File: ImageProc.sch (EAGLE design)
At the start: 114 parts, among them IC1 XC61GC3002HR-G, IC10 AT45DB642D-CNU, IC2 MIC5335-SPYMT, IC3 MIC5335-JGYMT, IC5 AT86RF233-ZU, IC6 LTC6088, IC7 DRV8833RTY, IC8 DRV8833RTY, IC9 MPU-6000, P1 BAT+, P10 MD2, P11 EXT1, P12 EXT2, P13 EXT3, P14 EXT4, P16 EXT5, P2 BAT-, P3 MA1, P4 MA2, P5 MB1, P6 MB2, P7 MC1, P8 MC2, P9 MD1, U1 CY8C5688LTI-LP086

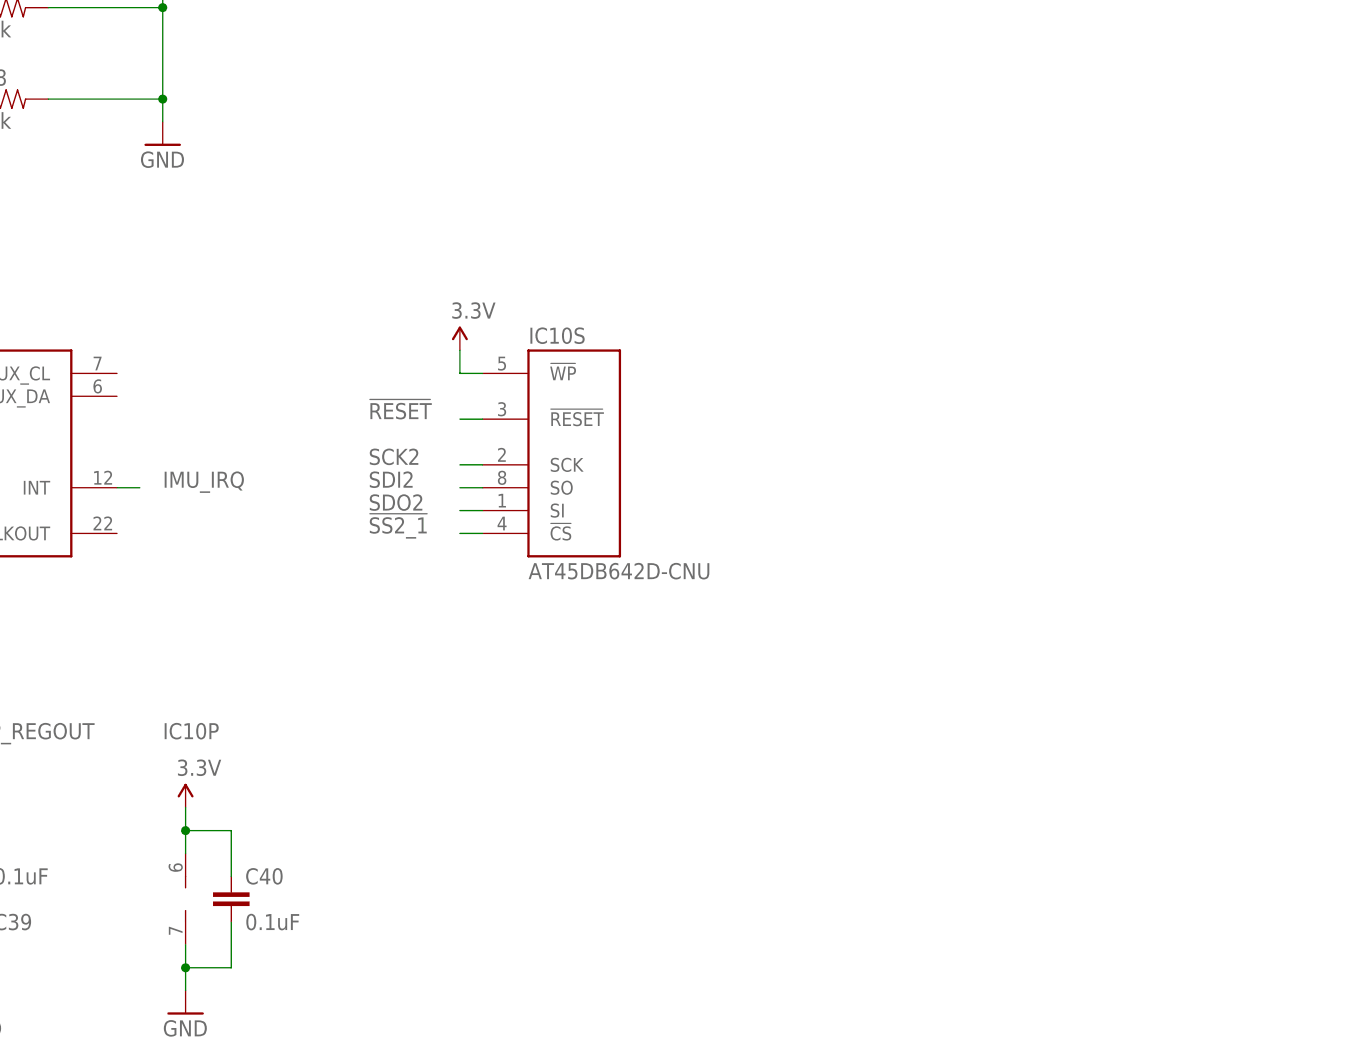
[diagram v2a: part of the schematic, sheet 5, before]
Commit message: Removed flash, ripping up more routing, added SD card
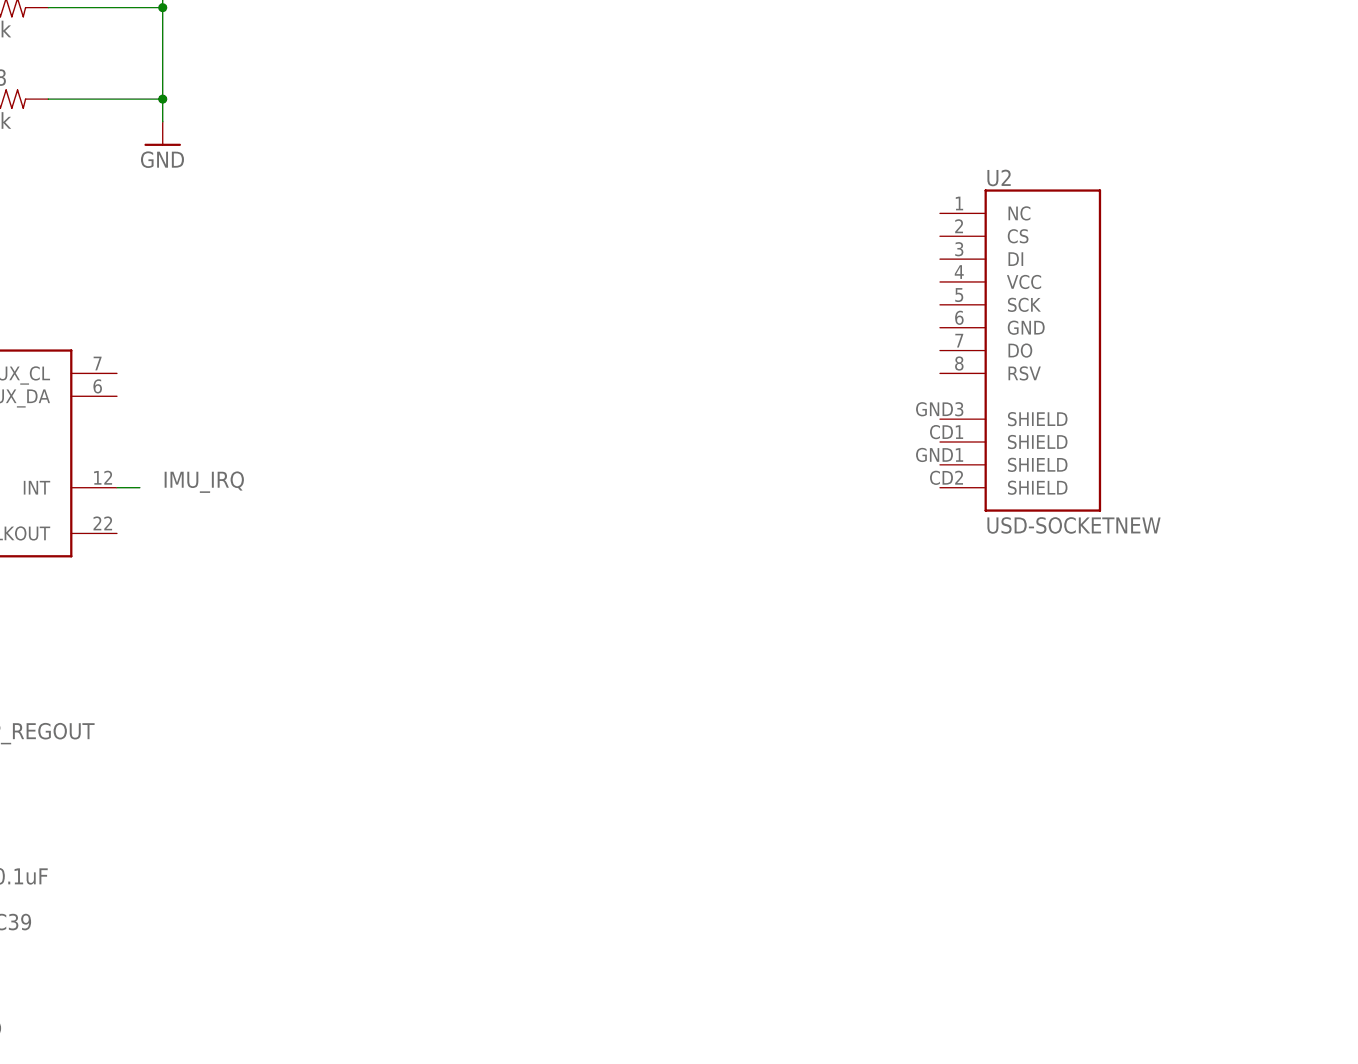
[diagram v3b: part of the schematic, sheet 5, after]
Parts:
- removed C40: 0.1uF, biomimetic:CAP0402-CAP
- removed IC10: AT45DB642D-CNU, biomimetic:AT45DB642D-CNU
- added U2: USD-SOCKETNEW, SparkFun-Connectors:USD-SOCKETNEW
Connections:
- removed net !SS2_1: IC10S.!CS
- net !RESET: no longer IC10S.!RESET
- net 3.3V: no longer C40.1, IC10P.V+, IC10S.!WP
- net GND: no longer C40.2, IC10P.V-
- net SCK2: no longer IC10S.SCK
- net SDI2: no longer IC10S.SO
- net SDO2: no longer IC10S.SI
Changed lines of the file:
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@@
 <layer number="108" name="tplace-old" color="10" fill="1" visible="no" active="yes"/>
 <layer number="109" name="ref-old" color="11" fill="1" visible="no" active="yes"/>
+<layer number="110" name="fp0" color="7" fill="1" visible="yes" active="yes"/>
+<layer number="111" name="LPC17xx" color="7" fill="1" visible="yes" active="yes"/>
+<layer number="112" name="tSilk" color="7" fill="1" visible="yes" active="yes"/>
+<layer number="113" name="IDFDebug" color="4" fill="1" visible="yes" active="yes"/>
 <layer number="116" name="Patch_BOT" color="9" fill="4" visible="no" active="yes"/>
 <layer number="121" name="_tsilk" color="7" fill="1" visible="no" active="yes"/>
 <layer number="122" name="_bsilk" color="7" fill="1" visible="no" active="yes"/>
+<layer number="123" name="tTestmark" color="7" fill="1" visible="yes" active="yes"/>
+<layer number="124" name="bTestmark" color="7" fill="1" visible="yes" active="yes"/>
 <layer number="125" name="_tNames" color="7" fill="1" visible="no" active="yes"/>
+<layer number="126" name="_bNames" color="7" fill="1" visible="yes" active="yes"/>
+<layer number="127" name="_tValues" color="7" fill="1" visible="yes" active="yes"/>
+<layer number="128" name="_bValues" color="7" fill="1" visible="yes" active="yes"/>
+<layer number="131" name="tAdjust" color="7" fill="1" visible="yes" active="yes"/>
+<layer number="132" name="bAdjust" color="7" fill="1" visible="yes" active="yes"/>
 <layer number="144" name="Drill_legend" color="7" fill="1" visible="no" active="yes"/>
+<layer number="150" name="Notes" color="7" fill="1" visible="yes" active="yes"/>
 <layer number="151" name="HeatSink" color="7" fill="1" visible="no" active="yes"/>
+<layer number="152" name="_bDocu" color="7" fill="1" visible="yes" active="yes"/>
+<layer number="153" name="FabDoc1" color="7" fill="1" visible="yes" active="yes"/>
+<layer number="154" name="FabDoc2" color="7" fill="1" visible="yes" active="yes"/>
+<layer number="155" name="FabDoc3" color="7" fill="1" visible="yes" active="yes"/>
 <layer number="199" name="Contour" color="7" fill="1" visible="yes" active="yes"/>
 <layer number="200" name="200bmp" color="1" fill="10" visible="no" active="yes"/>
@@
 <layer number="223" name="223bmp" color="24" fill="1" visible="no" active="no"/>
 <layer number="224" name="224bmp" color="25" fill="1" visible="no" active="no"/>
+<layer number="248" name="Housing" color="7" fill="1" visible="yes" active="yes"/>
+<layer number="249" name="Edge" color="7" fill="1" visible="yes" active="yes"/>
 <layer number="250" name="Descript" color="3" fill="1" visible="no" active="no"/>
 <layer number="251" name="SMDround" color="12" fill="11" visible="no" active="no"/>
@@
 <part name="P+8" library="biomimetic" deviceset="3.3V" device=""/>
 <part name="IC6" library="biomimetic" deviceset="LTC6088" device=""/>
-<part name="P+7" library="biomimetic" deviceset="3.3V" device=""/>
-<part name="C40" library="biomimetic" deviceset="CAP" device="0402-CAP" value="0.1uF"/>
 <part name="IC1" library="biomimetic" deviceset="XC61GC3002HR" device="-G"/>
 <part name="IC2" library="biomimetic" deviceset="MIC5335-SPYMT" device=""/>
 <part name="IC3" library="biomimetic" deviceset="MIC5335-JGYMT" device=""/>
-<part name="GND9" library="biomimetic" deviceset="GND" device=""/>
-<part name="P+10" library="biomimetic" deviceset="3.3V" device=""/>
 <part name="C35" library="biomimetic" deviceset="CAP" device="0402-CAP" value="2.2uF">
 <attribute name="TECHNOLOGY" value="CERAMIC"/>
@@
 <part name="GND49" library="biomimetic" deviceset="GND" device=""/>
 <part name="GND2" library="biomimetic" deviceset="GND" device=""/>
-<part name="IC10" library="biomimetic" deviceset="AT45DB642D" device="-CNU"/>
 <part name="IC9" library="biomimetic" deviceset="MPU-6000" device=""/>
 <part name="C3" library="biomimetic" deviceset="CAP" device="0402-CAP" value="0.1uF"/>
@@
 <part name="GND24" library="biomimetic" deviceset="GND" device=""/>
 <part name="U1" library="pullin" deviceset="CY8C5688LTI-LP086" device=""/>
+<part name="U2" library="SparkFun-Connectors" deviceset="USD-SOCKET" device="NEW"/>
 </parts>
 <sheets>
@@
 <instance part="R27" gate="G$1" x="50.8" y="119.38"/>
 <instance part="R28" gate="G$1" x="50.8" y="109.22"/>
-<instance part="P+7" gate="G$1" x="71.12" y="30.48"/>
-<instance part="C40" gate="G$1" x="76.2" y="20.32"/>
-<instance part="GND9" gate="1" x="71.12" y="7.62"/>
-<instance part="P+10" gate="G$1" x="101.6" y="81.28"/>
 <instance part="U$16" gate="G$1" x="152.4" y="167.64"/>
 <instance part="GND41" gate="1" x="152.4" y="142.24" smashed="yes">
@@
 <instance part="GND49" gate="1" x="48.26" y="7.62"/>
 <instance part="GND2" gate="1" x="68.58" y="104.14"/>
-<instance part="IC10" gate="S" x="114.3" y="68.58"/>
-<instance part="IC10" gate="P" x="71.12" y="20.32"/>
 <instance part="IC9" gate="S" x="45.72" y="68.58"/>
 <instance part="IC9" gate="P_VDD" x="10.16" y="20.32"/>
@@
 <instance part="P+1" gate="G$1" x="218.44" y="165.1"/>
 <instance part="GND24" gate="1" x="218.44" y="142.24"/>
+<instance part="U2" gate="G$1" x="162.56" y="83.82"/>
 </instances>
 <busses>
@@
 </segment>
 <segment>
-<pinref part="GND9" gate="1" pin="GND"/>
-<pinref part="IC10" gate="P" pin="V-"/>
-<wire x1="71.12" y1="10.16" x2="71.12" y2="12.7" width="0.1524" layer="91"/>
-<pinref part="C40" gate="G$1" pin="2"/>
-<wire x1="71.12" y1="12.7" x2="71.12" y2="15.24" width="0.1524" layer="91"/>
-<wire x1="71.12" y1="12.7" x2="76.2" y2="12.7" width="0.1524" layer="91"/>
-<wire x1="76.2" y1="12.7" x2="76.2" y2="17.78" width="0.1524" layer="91"/>
-<junction x="71.12" y="12.7"/>
-</segment>
-<segment>
 <pinref part="C38" gate="G$1" pin="1"/>
 <pinref part="GND15" gate="1" pin="GND"/>
@@
 <net name="SDO2" class="0">
 <segment>
-<wire x1="104.14" y1="63.5" x2="101.6" y2="63.5" width="0.1524" layer="91"/>
-<label x="91.44" y="63.5" size="1.778" layer="95"/>
-<pinref part="IC10" gate="S" pin="SI"/>
-</segment>
-<segment>
 <wire x1="27.94" y1="73.66" x2="25.4" y2="73.66" width="0.1524" layer="91"/>
 <label x="10.16" y="73.66" size="1.778" layer="95"/>
@@
 <net name="SCK2" class="0">
 <segment>
-<wire x1="104.14" y1="68.58" x2="101.6" y2="68.58" width="0.1524" layer="91"/>
-<label x="91.44" y="68.58" size="1.778" layer="95"/>
-<pinref part="IC10" gate="S" pin="SCK"/>
-</segment>
-<segment>
 <pinref part="IC9" gate="S" pin="SCL/SCLK"/>
 <wire x1="27.94" y1="78.74" x2="25.4" y2="78.74" width="0.1524" layer="91"/>
@@
 <net name="SDI2" class="0">
 <segment>
-<wire x1="104.14" y1="66.04" x2="101.6" y2="66.04" width="0.1524" layer="91"/>
-<label x="91.44" y="66.04" size="1.778" layer="95"/>
-<pinref part="IC10" gate="S" pin="SO"/>
-</segment>
-<segment>
 <wire x1="27.94" y1="76.2" x2="25.4" y2="76.2" width="0.1524" layer="91"/>
 <label x="10.16" y="76.2" size="1.778" layer="95"/>
@@
 </segment>
 </net>
-<net name="!SS2_1" class="0">
-<segment>
-<wire x1="104.14" y1="60.96" x2="101.6" y2="60.96" width="0.1524" layer="91"/>
-<label x="91.44" y="60.96" size="1.778" layer="95"/>
-<pinref part="IC10" gate="S" pin="!CS"/>
-</segment>
-</net>
 <net name="N$15" class="0">
 <segment>
@@
 <net name="!RESET" class="0">
 <segment>
-<wire x1="104.14" y1="73.66" x2="101.6" y2="73.66" width="0.1524" layer="91"/>
-<label x="91.44" y="73.66" size="1.778" layer="95"/>
-<pinref part="IC10" gate="S" pin="!RESET"/>
-</segment>
-<segment>
 <pinref part="JP1" gate="G$1" pin="5"/>
 <wire x1="109.22" y1="149.86" x2="121.92" y2="149.86" width="0.1524" layer="91"/>
@@
 </net>
 <net name="3.3V" class="0">
-<segment>
-<wire x1="104.14" y1="78.74" x2="101.6" y2="78.74" width="0.1524" layer="91"/>
-<wire x1="101.6" y1="78.74" x2="101.6" y2="81.28" width="0.1524" layer="91"/>
-<pinref part="P+10" gate="G$1" pin="3.3V"/>
-<pinref part="IC10" gate="S" pin="!WP"/>
-</segment>
 <segment>
 <pinref part="P+4" gate="G$1" pin="3.3V"/>
@@
 </segment>
 <segment>
-<pinref part="IC10" gate="P" pin="V+"/>
-<pinref part="P+7" gate="G$1" pin="3.3V"/>
-<wire x1="71.12" y1="25.4" x2="71.12" y2="27.94" width="0.1524" layer="91"/>
-<pinref part="C40" gate="G$1" pin="1"/>
-<wire x1="71.12" y1="27.94" x2="71.12" y2="30.48" width="0.1524" layer="91"/>
-<wire x1="71.12" y1="27.94" x2="76.2" y2="27.94" width="0.1524" layer="91"/>
-<wire x1="76.2" y1="27.94" x2="76.2" y2="22.86" width="0.1524" layer="91"/>
-<junction x="71.12" y="27.94"/>
-</segment>
-<segment>
